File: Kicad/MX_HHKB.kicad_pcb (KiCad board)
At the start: 2 copper layers, 285.8 x 95.2 mm, 136 parts, among them J1 USB_mini_micro_B, K1 Esc, K10 9, K11 0, K12 -, K13 =, K14 Tab, K15 Q, K16 W, K17 E, K18 R, K19 T, K2 1, K20 Y, K21 U, K22 I, K23 O, K24 P, K25 [, K26 ], K27 Ctrl, K28 A, K29 S, K3 2, K30 D, K31 F, K32 G, K33 H, K34 J, K35 K, K36 L, K37 ;, K38 ', K39 Enter, K4 3, K40 L_Shift, K41 Z, K42 X, K43 C, K44 V, K45 B, K46 N, K47 M, K48 ,, K49 ., K5 4, K50 /, K51 R_Shift, K52 Fn, K53 L_GUI, K54 L_ALT, K55 SPACE, K56 R_ALT, K57 R_GUI, K58 \, K59 `, K6 5, K60 BACKSPACE, K7 6, K8 7, K9 8, SW1 SW_PUSH, U0 ATMEGA32U4, X1 XTAL_GND

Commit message: - Updated position of Atmega and Crystal - Added render view
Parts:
- K39: footprint Fooprints:Mx_Alps_225 -> Footprint:Mx_Alps_225
- K55: footprint Fooprints:Mx_Alps_625 -> Footprint:Mx_Alps_625
- moved C2 57.7 mm to (101.0, 179.2), turned to 90 degrees
- moved C1 57.0 mm to (91.2, 189.2), turned to 180 degrees
- moved X1 53.8 mm to (99.2, 186.8), turned to 45 degrees
- moved K58 19.0 mm to (342.9, 107.2)
- moved K59 19.0 mm to (323.9, 107.2)
- moved D27 16.9 mm to (96.5, 137.8)
- moved D59 11.2 mm to (333.4, 109.5), turned to 90 degrees
- moved D58 9.82 mm to (342.9, 111.9), turned to 0 degrees
- moved D1 5.95 mm to (82.2, 112.0), turned to 135 degrees
- moved C8 3.20 mm to (96.2, 168.5), turned to 90 degrees
- moved R3 2.30 mm to (70.5, 122.0)
- moved R4 1.77 mm to (73.2, 126.5)
- moved U0 1.03 mm to (82.0, 178.5)
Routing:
- net /Row0: track 313.8 -> 456.6 mm
- net Net-(C2-Pad1): track 95.8 -> 20.6 mm, vias 4 -> 2
- net Net-(C1-Pad1): track 75.3 -> 18.5 mm, vias 4 -> 0
- net /Row2: track 315.7 -> 366.1 mm
- net /Row1: track 289.2 -> 319.0 mm, vias 4 -> 1
- net /Col8: track 328.8 -> 301.6 mm, vias 5 -> 7
- net /Col11: track 380.3 -> 353.2 mm, vias 6 -> 1
- net /Col9: track 355.5 -> 330.7 mm, vias 7 -> 5
- net GND: track 223.6 -> 246.7 mm, vias 9 -> 0
- net /Col2: track 155.8 -> 140.6 mm, vias 4 -> 3
- net /Row3: track 281.5 -> 266.9 mm, vias 6 -> 3
- net /Col4: track 201.6 -> 192.8 mm, vias 1 -> 3
- net /Row4: track 352.8 -> 361.5 mm, vias 0 -> 3
- net /Col5: track 228.8 -> 235.8 mm, vias 7 -> 4
- net /Col3: track 140.2 -> 146.9 mm, vias 3 -> 4
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
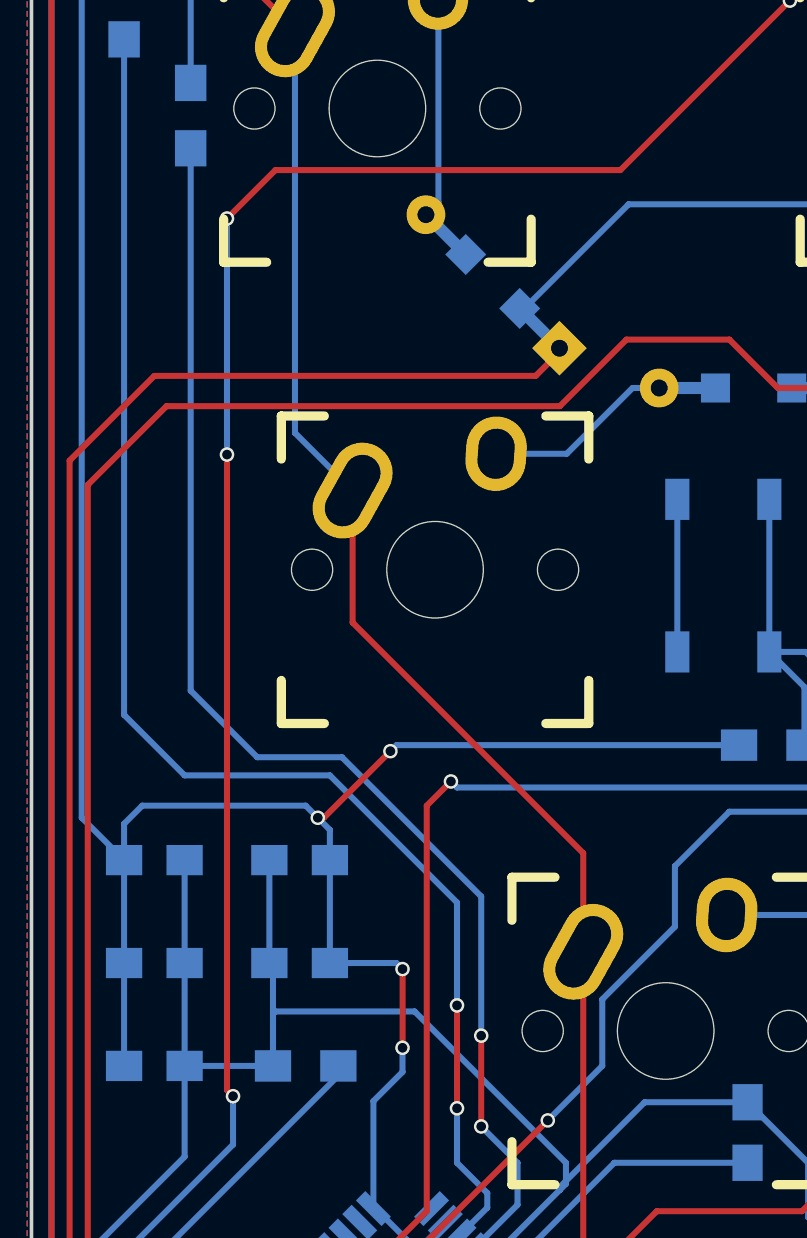
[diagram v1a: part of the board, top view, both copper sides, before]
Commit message: - Added 175 stepped Ctrontrol key
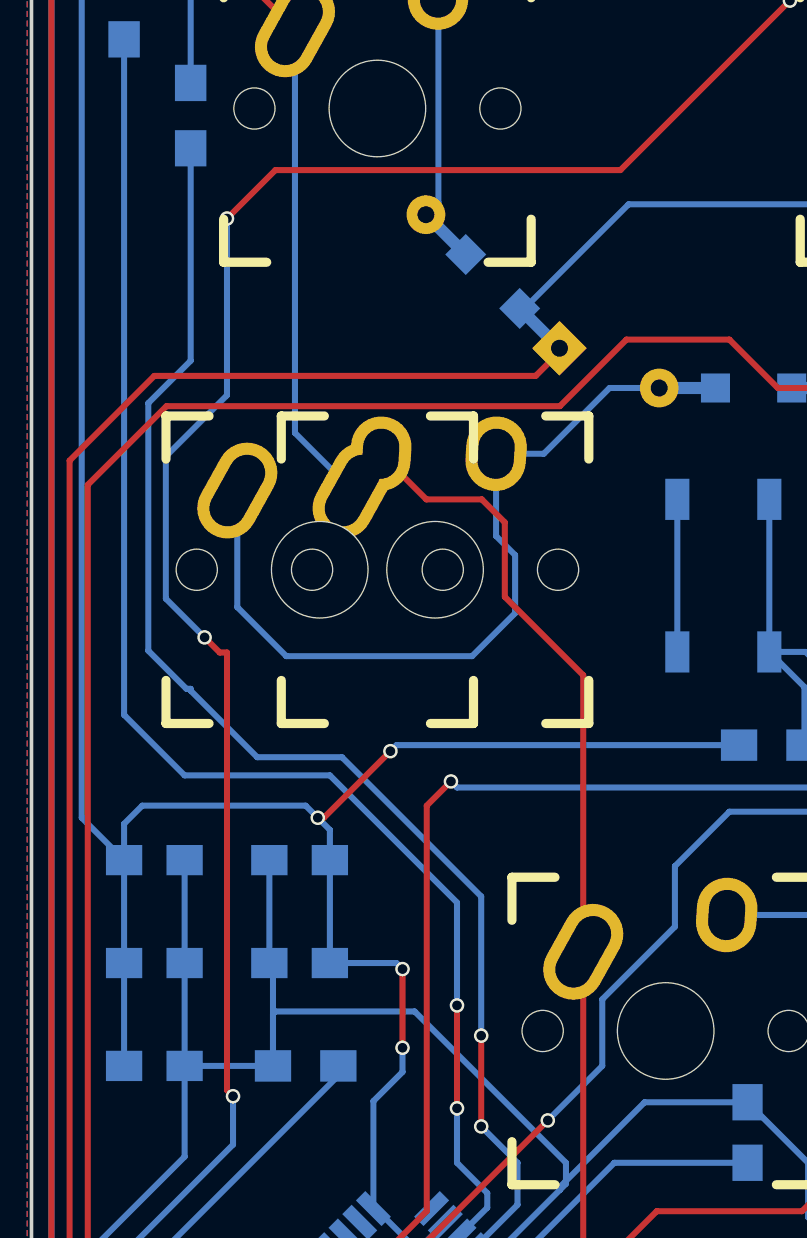
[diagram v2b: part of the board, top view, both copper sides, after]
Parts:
- added K61: Ctrl, Footprint:Mx_Alps_175_STEPPED, F.Cu at (78.6, 145.3)
- K58: value \ -> `
- K59: value ` -> \
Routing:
- net Net-(D27-Pad2): track 7.86 -> 32.6 mm
- net /Col0: track 79.6 -> 83.9 mm
- net /Col6: track 245.9 -> 248.2 mm
- net Net-(R4-Pad2): track 53.9 -> 55.4 mm

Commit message: - Added Poker Hole - Added Poker plate (dxf and svg) - Updated render and layout preview
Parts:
- added HOLE_M3: VAL**, Footprint:HOLE_M3, F.Cu at (92.3, 125.3)
- added Poker_oval_hole: VAL**, Footprint:Poker_oval_hole, F.Cu at (327.1, 125.4)
- added Poker_oval_hole: VAL**, Footprint:Poker_oval_hole, F.Cu at (257.3, 182.7)
- added Poker_oval_hole: VAL**, Footprint:Poker_oval_hole, F.Cu at (195.2, 144.8)
- added Poker_side_edge_long: VAL**, Footprint:Poker_side_edge_long, F.Cu at (66.1, 153.8)
- added Poker_side_edge_long: VAL**, Footprint:Poker_side_edge_long, F.Cu at (353.1, 153.8)
- moved C3 11.1 mm to (71.6, 168.3)
- moved D32 4.22 mm to (192.5, 150.8), turned to 180 degrees
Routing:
- net /Row2: track 366.1 -> 371.4 mm
- net /Row1: track 319.0 -> 323.8 mm
- net /Col6: track 248.2 -> 252.8 mm
- net /Row0: track 456.6 -> 460.7 mm
- net VCC: track 167.5 -> 171.3 mm
- net /Row4: track 361.5 -> 364.7 mm
- net Net-(R3-Pad1): track 59.6 -> 57.2 mm
- net Net-(D32-Pad2): track 8.36 -> 10.5 mm
- net GND: track 246.7 -> 248.2 mm
- net /Col12: track 359.6 -> 360.7 mm
- net Net-(R4-Pad2): track 55.4 -> 54.4 mm
